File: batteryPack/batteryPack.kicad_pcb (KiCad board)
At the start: 2 copper layers, 204 x 78 mm, 38 parts, among them J1 USB_B_Micro, J10 B1+, J11 B1-, J12 B2-, J13 B1+, J14 B1-, J15 B2+, J16 B2-, J2 B1+, J3 B1-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

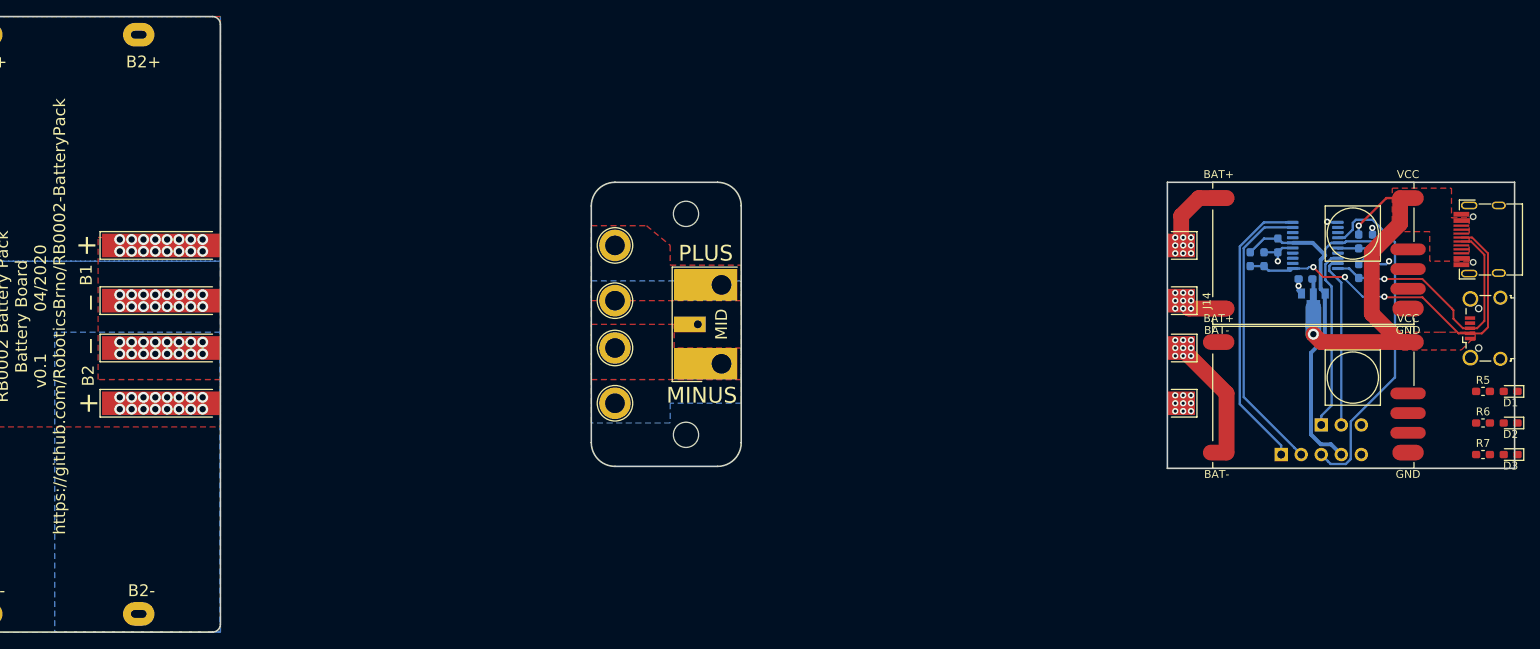
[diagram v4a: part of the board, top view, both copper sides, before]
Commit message: Make the labels nice
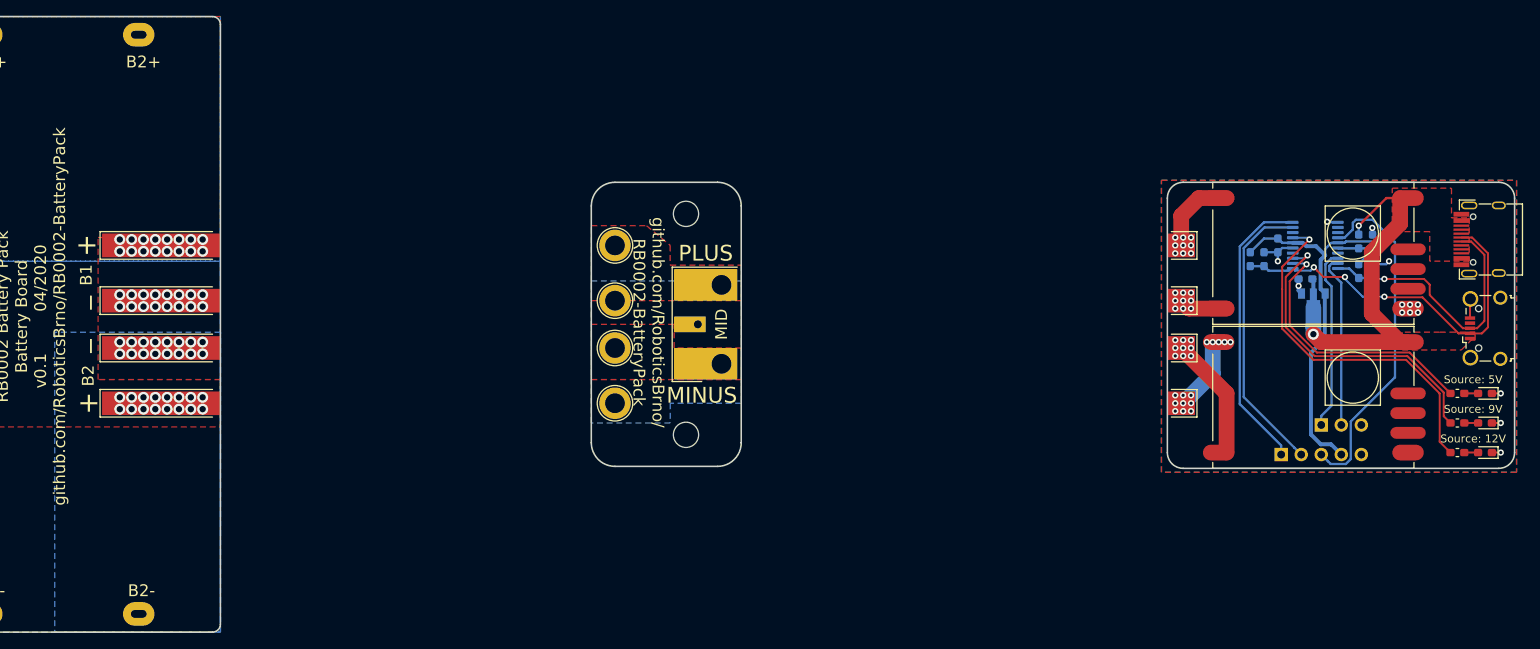
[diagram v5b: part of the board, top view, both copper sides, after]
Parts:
- moved D1 3.26 mm to (230.2, 78.8)
- moved D3 3.26 mm to (230.2, 86.2)
- moved R5 3.26 mm to (226.8, 78.8)
- moved R7 3.26 mm to (226.8, 86.2)
- moved D2 3.25 mm to (230.2, 82.5)
- moved R6 3.25 mm to (226.8, 82.5)
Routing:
- net Net-(R7-Pad1): track 0.00 -> 46.4 mm, vias 0 -> 1
- net Net-(R6-Pad1): track 0.00 -> 40.0 mm, vias 0 -> 1
- net Net-(R5-Pad1): track 0.00 -> 34.4 mm, vias 0 -> 1
- net Net-(J15-Pad1): track 0.00 -> 10.8 mm, vias 9 -> 14
- net GND: track 11.5 -> 17.9 mm, vias 5 -> 14
- net Net-(D3-Pad2): track 0.00 -> 1.75 mm
- net Net-(D2-Pad2): track 0.00 -> 1.75 mm
- net Net-(D1-Pad2): track 0.00 -> 1.75 mm
- added copper zone on B.Cu, net GND
- added copper zone on F.Cu, net GND
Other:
- outline, holes or cut-outs redrawn
- board text added: "GND 3V3 RST IO CLK"
- board text added: "GND RX TX"
- board text added: "RB0002 Battery Pack Battery Board v0.1 04/2020 github.com/RoboticsBrno/RB0002-BatteryPack"
- board text added: "RB0002 Battery Pack Charger v0.1 04/2020"
- board text added: "RB0002 Battery Pack Connector v0.1"
- board text added: "Source: 12V"
- board text added: "Source: 5V"
- board text added: "Source: 9V"
- board text added: "github.com/RoboticsBrno/ RB0002-BatteryPack"
- board text removed: "RB0002 Battery Pack Battery Board v0.1 04/2020 https://github.com/RoboticsBrno/RB0002-BatteryPack"
